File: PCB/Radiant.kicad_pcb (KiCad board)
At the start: 2 copper layers, 94.5 x 88.6 mm, 20 parts, among them J1 Conn_01x04, SW1 RotaryEncoder_Switch, SW5 SW_Push, SW6 SW_Push, SW7 SW_Push, SW8 SW_Push, U1 XIAO-ESP32-C3-DIP

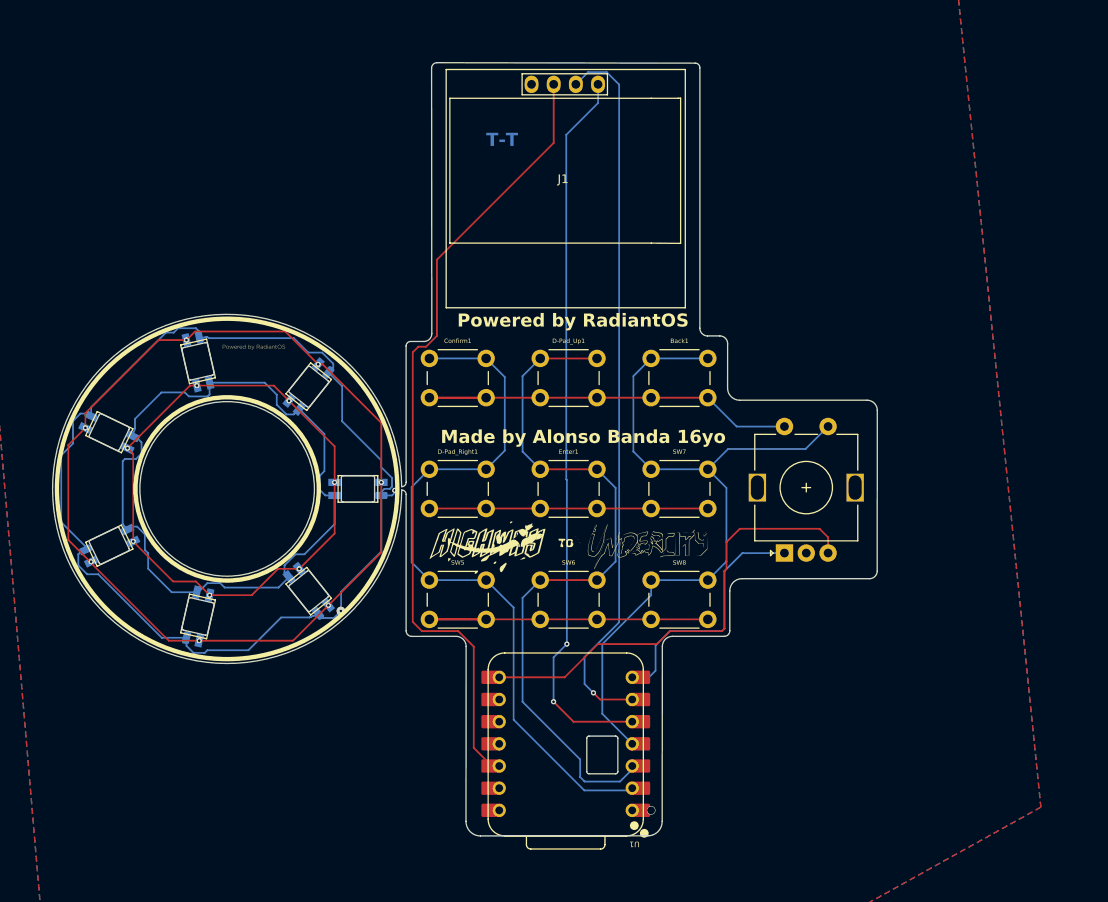
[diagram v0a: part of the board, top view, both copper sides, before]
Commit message: Redesigned pcb and made case design
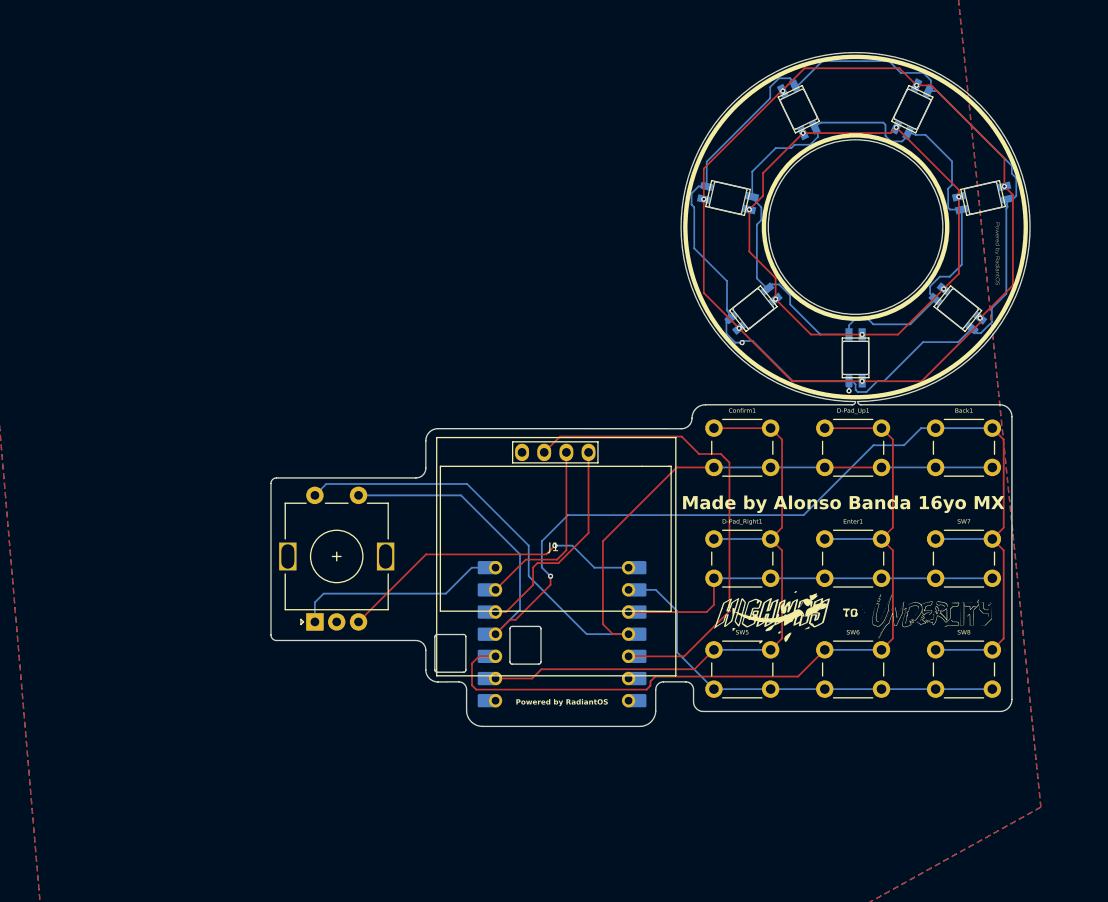
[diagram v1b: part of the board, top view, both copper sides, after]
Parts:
- U1: moved to B.Cu
- moved D1 99.2 mm to (126.5, 83.5), turned to 64.285 degrees
- moved D1 93.5 mm to (113.4, 83.5), turned to 115.714 degrees
- moved D1 91.9 mm to (134.6, 93.7), turned to 12.857 degrees
- moved D1 77.4 mm to (105.3, 93.7), turned to 167.143 degrees
- moved D1 74.9 mm to (131.7, 106.3), turned to -38.571 degrees
- moved D1 60.4 mm to (108.2, 106.3), turned to -141.428 degrees
- moved D1 59.0 mm to (119.9, 112.0), turned to -90 degrees
- moved SW1 54.4 mm to (58.0, 142.2)
- moved J1 42.2 mm to (85.4, 133.4)
- moved Back1 33.6 mm to (129.1, 120.0)
- moved D-Pad_Up1 33.6 mm to (116.4, 120.0)
- moved Enter1 33.6 mm to (116.4, 132.7)
- moved SW6 33.6 mm to (116.4, 145.4)
- moved SW7 33.6 mm to (129.1, 132.7)
- moved SW8 33.6 mm to (129.1, 145.4)
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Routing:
- net SCL: track 83.5 -> 21.2 mm, vias 1 -> 0
- net Row1: track 48.5 -> 107.5 mm
- net SDA: track 82.9 -> 24.8 mm, vias 2 -> 0
- net Colum3: track 86.7 -> 143.2 mm, vias 0 -> 1
- net 3v3: track 91.5 -> 53.9 mm
- net EC-B: track 52.6 -> 35.6 mm, vias 0 -> 1
- net Colum2: track 81.6 -> 95.4 mm
- net Row2: track 31.9 -> 45.1 mm
- net Row3: track 38.4 -> 48.3 mm
- net Colum1: track 82.7 -> 73.4 mm
- net EC-A: track 28.9 -> 23.7 mm
- net Net-(D1-DIN): track 130.8 -> 128.8 mm, vias 3 -> 2
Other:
- board size 94.5 x 88.6 mm -> 87 x 77.2 mm
- board text added: "Made by Alonso Banda 16yo MX"
- board text removed: "Made by Alonso Banda 16yo"
- board text removed: "T-T"

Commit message: Updated RadiantOS
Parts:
- J1: value Conn_01x04 -> Display 128*64
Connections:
- net Net-(D1-VDD) renamed VOUT+
- D1 pad 2: Net-(D1-VSS) -> GND (x7)
- U1 pad 14: 5V+ -> unconnected-(U1-VBUS-Pad14)
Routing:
- net GND: track 0.00 -> 95.1 mm, vias 0 -> 2
- net Net-(D1-VSS): track 89.4 -> 0.00 mm
- net Row3: track 48.3 -> 49.5 mm
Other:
- outline, holes or cut-outs redrawn
- board text added: "+"
- board text added: "-"
- board text added: "DATA"
- board text added: "GND"
- board text added: "VOUT+"
- board text added: "| V"
